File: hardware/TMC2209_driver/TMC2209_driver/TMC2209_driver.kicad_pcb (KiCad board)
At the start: 2 copper layers, 21 parts, among them J1 Conn_01x08, J2 Conn_01x08, J3 Conn_01x02

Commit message: finished driver board design
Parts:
- removed C8: 10µF, Capacitor_SMD:C_1206_3216Metric
- C1, C2, C3, C4, C5, C9: footprint Capacitor_SMD:C_0603_1608Metric -> Capacitor_SMD:C_0402_1005Metric
- JP1: footprint Jumper:SolderJumper-3_P1.3mm_Open_Pad1.0x1.5mm -> FlexPrint:SolderJumper_3Pads
- R1, R2, R6: footprint Resistor_SMD:R_0603_1608Metric -> Resistor_SMD:R_0402_1005Metric
- R4, R5: footprint Resistor_SMD:R_1206_3216Metric -> Resistor_SMD:R_0805_2012Metric
- RV1: footprint Potentiometer_SMD:Potentiometer_Bourns_3314J_Vertical -> FlexPrint:TRIMMER_3312J-1-203E; moved to B.Cu
- TP1: moved to B.Cu
- moved C1 40.7 mm to (153.9, 93.0), turned to 90 degrees
- moved C4 39.9 mm to (152.4, 96.3), turned to -90 degrees
- moved C5 39.1 mm to (152.4, 103.7), turned to 90 degrees
- moved C9 39.1 mm to (148.8, 93.5), turned to -90 degrees
- moved R6 39.0 mm to (150.5, 105.5), turned to 90 degrees
- moved C3 37.2 mm to (150.0, 95.5), turned to -90 degrees
- moved R2 35.1 mm to (146.0, 102.0), turned to -90 degrees
- moved C2 34.4 mm to (147.6, 95.5), turned to 90 degrees
- moved R1 33.3 mm to (146.0, 105.5), turned to -90 degrees
- moved TP1 24.3 mm to (153.9, 106.0), turned to 180 degrees
- moved R4 23.2 mm to (153.9, 97.8), turned to 90 degrees
- moved JP1 21.8 mm to (145.0, 97.1), turned to -90 degrees
- moved RV1 20.9 mm to (152.7, 108.2), turned to 90 degrees
- moved C7 13.0 mm to (152.4, 91.0), turned to 180 degrees
- moved C6 12.9 mm to (147.8, 91.0)
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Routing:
- net VM: track 0.00 -> 22.2 mm, vias 0 -> 3
- net Net-(U2-VREF): track 0.00 -> 11.0 mm, vias 0 -> 1
- net VIO: track 0.00 -> 7.04 mm
- net PDN_UART: track 0.00 -> 6.67 mm
- net GND: track 0.00 -> 5.16 mm, vias 0 -> 103
- net Net-(U2-VCP): track 0.00 -> 3.69 mm
- net EN: track 0.00 -> 3.48 mm
- net Net-(R6-Pad1): track 0.00 -> 3.43 mm, vias 0 -> 1
- net Net-(U2-CPI): track 0.00 -> 3.02 mm
- net +5V: track 0.00 -> 2.52 mm
- net Net-(J1-Pin_3): track 0.00 -> 2.04 mm
- net Net-(J1-Pin_4): track 0.00 -> 1.99 mm
- net Net-(U2-BRA): track 0.00 -> 1.74 mm
- net Net-(U2-CPO): track 0.00 -> 1.59 mm
- net Net-(U2-BRB): track 0.00 -> 1.54 mm
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- added copper zone on B.Cu, net GND
- added copper zone on F.Cu, net GND
- added copper zone on F.Cu, net OUTA1
- added copper zone on F.Cu, net OUTA2
- added copper zone on F.Cu, net OUTB1
- added copper zone on F.Cu, net OUTB2
- added copper zone on F.Cu, net VM

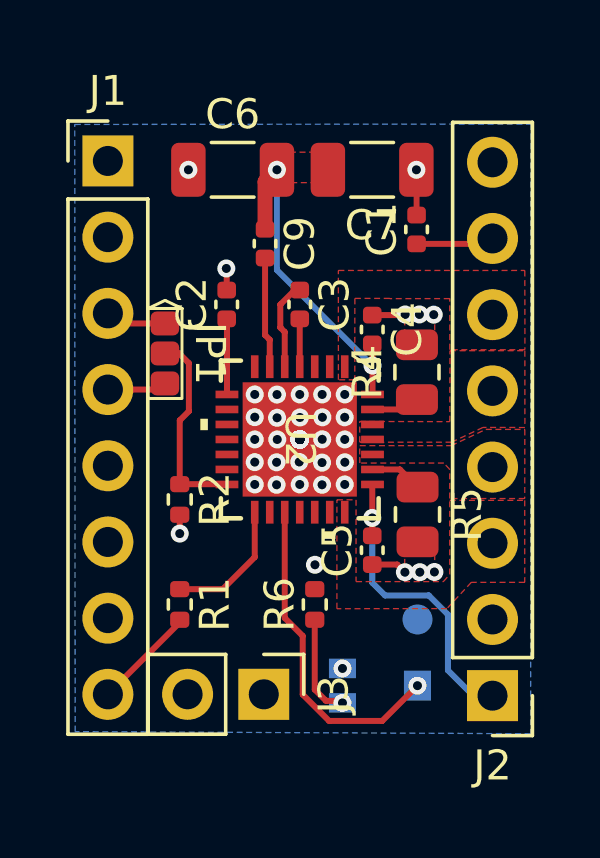
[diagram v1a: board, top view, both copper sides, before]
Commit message: driver board finalized, mainboard started placing FET drivers
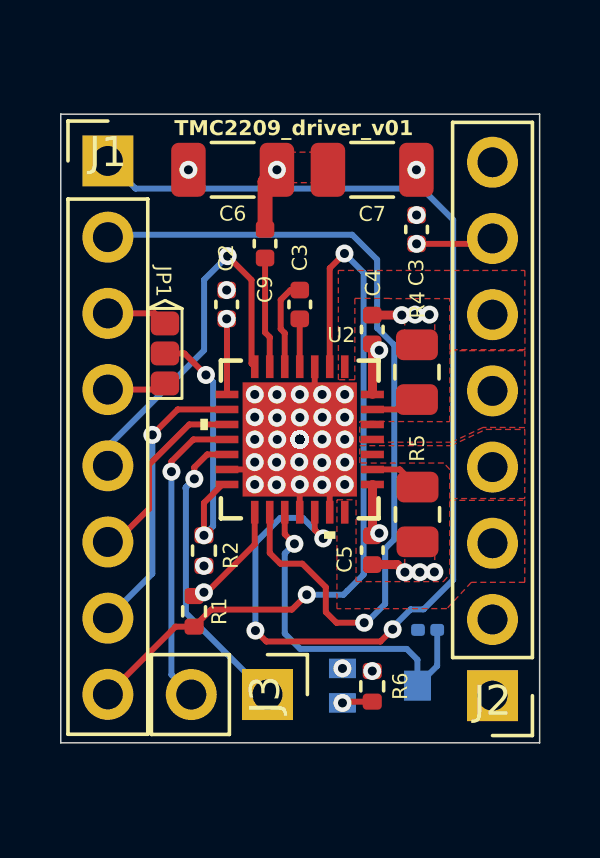
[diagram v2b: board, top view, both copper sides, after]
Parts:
- TP1: footprint TestPoint:TestPoint_Pad_D1.0mm -> Resistor_SMD:R_0201_0603Metric
- moved R6 3.34 mm to (152.4, 108.2)
- moved R2 1.89 mm to (146.8, 103.7)
- moved R1 0.53 mm to (146.5, 105.7)
- moved TP1 0.48 mm to (154.3, 106.3)
- moved J3 0.12 mm to (148.9, 108.5)
- renumbered C1 to C3
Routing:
- net DIR: track 0.00 -> 38.8 mm, vias 0 -> 3
- net STEP: track 0.00 -> 28.1 mm, vias 0 -> 1
- net VIO: track 7.04 -> 33.0 mm, vias 0 -> 2
- net EN: track 3.48 -> 25.1 mm, vias 0 -> 2
- net +5V: track 2.52 -> 16.6 mm, vias 0 -> 2
- net SPREAD: track 0.00 -> 12.7 mm, vias 0 -> 1
- net INDEX: track 0.00 -> 11.4 mm, vias 0 -> 1
- net DIAG: track 0.00 -> 10.2 mm, vias 0 -> 1
- net MS1: track 0.00 -> 9.56 mm, vias 0 -> 1
- net MS2: track 0.00 -> 6.45 mm
- net VM: track 22.2 -> 27.1 mm
- net PDN_UART: track 6.67 -> 9.34 mm, vias 0 -> 2
- net Net-(R6-Pad1): track 3.43 -> 1.01 mm
- net Net-(U2-VREF): track 11.0 -> 12.1 mm
- net GND: track 5.16 -> 6.18 mm, vias 103 -> 104
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- added copper zone on In1.Cu, net GND
- removed copper zone on B.Cu, net GND
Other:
- board outline added: 16 x 21 mm
- copper layers 2 -> 4
- board text added: "TMC2209_driver_v01"

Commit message: Mainboard-3
Version 3 of Mainboard, (version 2 not uploaded)
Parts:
- renumbered C3 to C1
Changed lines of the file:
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@@
 		(descr "Capacitor SMD 0402 (1005 Metric), square (rectangular) end terminal, IPC_7351 nominal, (Body size source: IPC-SM-782 page 76, https://www.pcb-3d.com/wordpress/wp-content/uploads/ipc-sm-782a_amendment_1_and_2.pdf), generated with kicad-footprint-generator")
 		(tags "capacitor")
-		(property "Reference" "C3"
+		(property "Reference" "C1"
 			(at -1.433925 -0.00922 90)
 			(layer "F.SilkS")
